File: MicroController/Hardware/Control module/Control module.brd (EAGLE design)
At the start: 100 x 60 mm, 90 parts, among them CN1 JST-PH_2-PIN_HEADER, CN2 JST-PH_2-PIN_HEADER, CN3 JST-PH_2-PIN_HEADER, CN4 JST-PH_2-PIN_HEADER, CN5 JST-PH_2-PIN_HEADER, CN6 JST-PH_2-PIN_HEADER, CN7 JST-PH_2-PIN_HEADER, CN8 JST-PH_2-PIN_HEADER, J1 1X2-3.5MM, J2 RJ45-TRAFO, J3 RJ45-TRAFO, J4 RJ45-TRAFO, J6 RJ11, Q1 BSS138, Q2 BSS138, Q3 BSS138, Q4 BSS138, Q5 BSS138, Q6 BSS138, Q7 BSS138, Q8 BSS138, U1 CD74HC4067SM96, U2 DUAL-OPTOISOLATOR_SOIC8, U3 TLV1117-33CDCY, U4 DUAL-OPTOISOLATOR_SOIC8

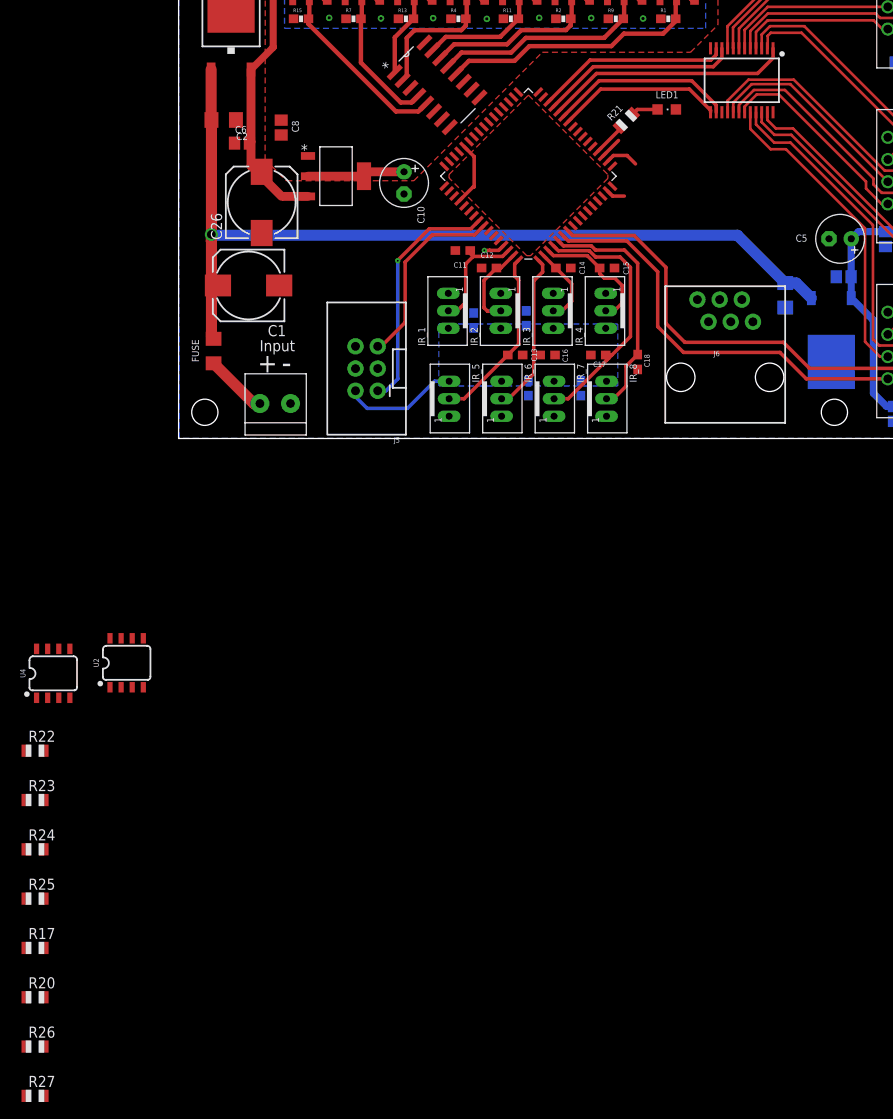
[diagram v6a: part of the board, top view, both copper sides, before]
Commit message: Added the possibility for remote programming.
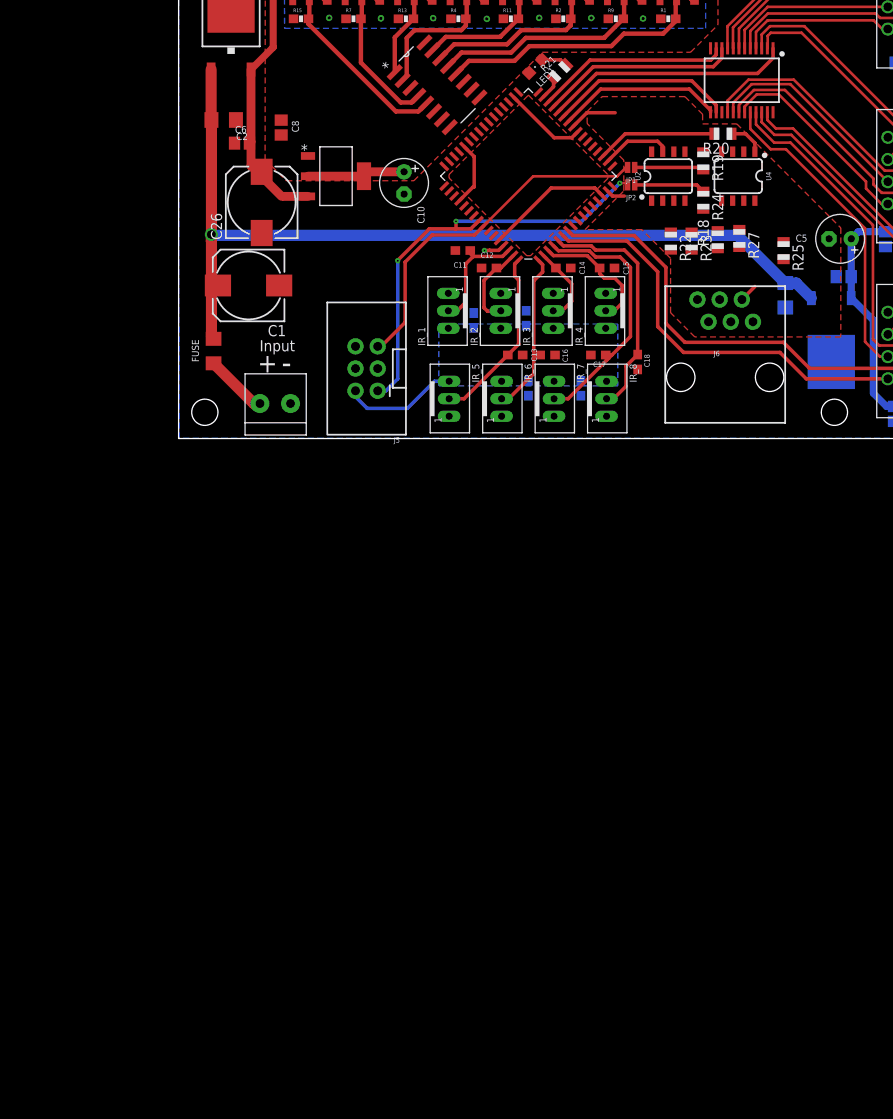
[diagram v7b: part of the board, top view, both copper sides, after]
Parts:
- removed R17, R26: 10K, adafruit:R0805
- added JP1, JP2: JUMPER-SMT_2_NO_NO-SILK, SparkFun-Jumpers:SMT-JUMPER_2_NO_NO-SILK
- added R18, R19: 10K, adafruit:R0805
- moved R27 126.9 mm to (64.1, 22.9), turned to 270 degrees
- moved R20 126.3 mm to (62.2, 34.9), turned to 180 degrees
- moved R25 113.2 mm to (69.2, 21.5), turned to 270 degrees
- moved R24 106.5 mm to (60.0, 27.2), turned to 270 degrees
- moved R23 98.6 mm to (58.7, 22.6), turned to 270 degrees
- moved U4 96.8 mm to (64.0, 30.0), turned to 180 degrees
- moved R22 93.2 mm to (56.3, 22.6), turned to 270 degrees
- moved U2 83.3 mm to (56.0, 30.0)
- moved LED1 15.8 mm to (40.8, 42.6), turned to 135 degrees
- moved R21 9.45 mm to (43.6, 42.0)
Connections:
- removed net N$3 (its old number): R21.2, U$1.20
- removed net SIGNAL_ATXMEGA: R17.2
- removed net SIGNAL_RASPI: J6.5, R26.1, U4.8
- new net DATA_RASPI: J6.5, R25.2
- new net N$1: R21.2, U$1.31
- new net N$4: R20.1, U4.1
- new net N$5: R25.1, U4.3
- net GND: now also R18.1, R19.1, R24.2; no longer U2.5, U2.7, U4.4
- net GND_RASPI: now also R27.2, U4.4; no longer U4.5, U4.7
- net N$2: now also JP1.1, R19.2, U2.5; no longer R17.1, U4.1
- net N$8: now also JP2.1, R24.1, U4.5; no longer R20.1, U4.3
- net PDI_DATA: now also JP2.2
- net RESET_PDI_CLK: now also JP1.2; no longer R24.1, U2.6
- net RX_ATXMEGA: now also R18.2, U2.7; no longer R25.1, U2.8
- net RX_RASPI: now also U4.7; no longer U4.6
- net VCC: now also U2.6, U2.8, U4.6; no longer R24.2, R25.2, R26.2, R27.2
- net VCC_RASPI: now also U4.8
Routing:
- net GND: track 7.49 -> 31.8 mm
- net PDI_DATA: track 27.6 -> 50.0 mm, vias 1 -> 3
- net RESET_PDI_CLK: track 21.9 -> 41.1 mm
- net TX_ATXMEGA: track 2.58 -> 13.8 mm
- net N$8: track 0.00 -> 8.15 mm
- net N$2: track 0.00 -> 7.95 mm
- net VCC: track 29.0 -> 34.5 mm
- net RX_ATXMEGA: track 3.87 -> 8.12 mm
- net N$4: track 0.00 -> 4.08 mm
- net N$3 (its old number): track 3.91 -> 0.00 mm
- net N$1: track 0.00 -> 2.70 mm
- net DATA_RASPI: track 0.00 -> 2.11 mm

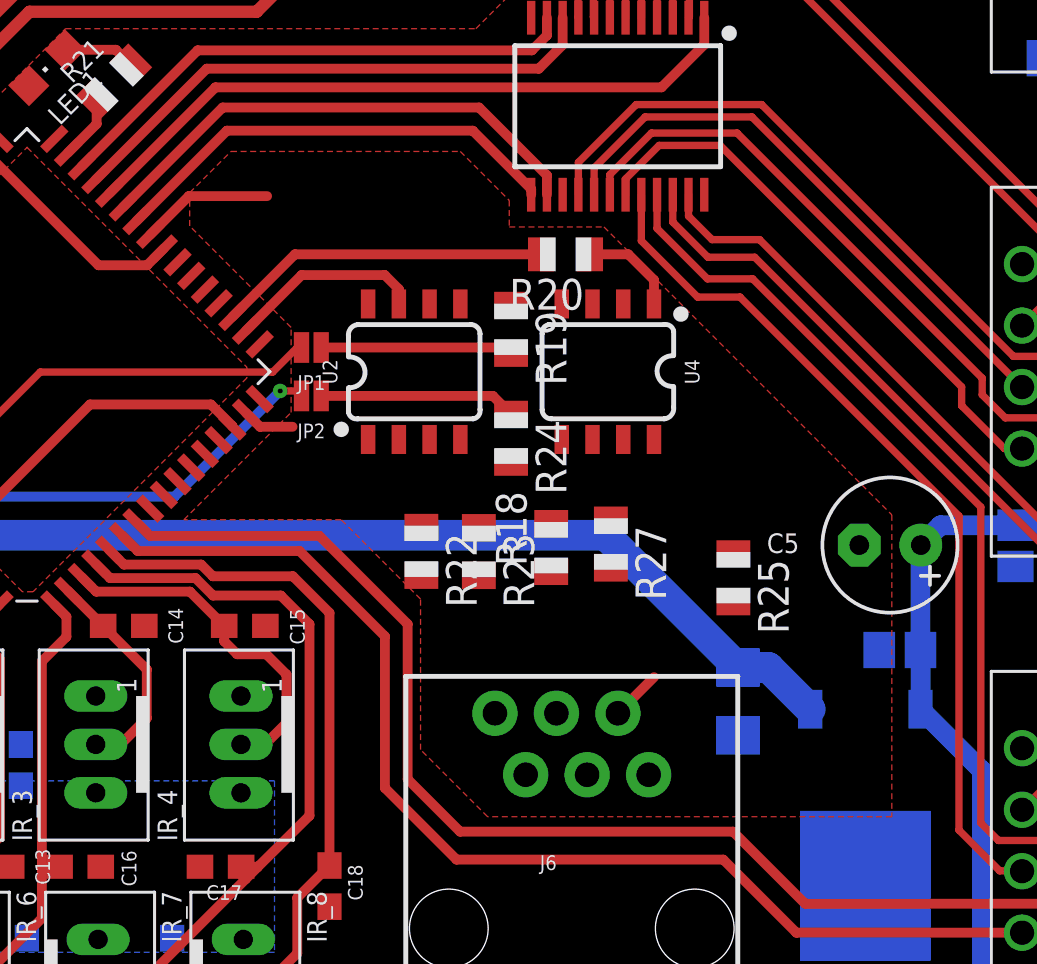
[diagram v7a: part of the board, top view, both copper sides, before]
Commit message: Communication line uses optocouplers for signal seperation.
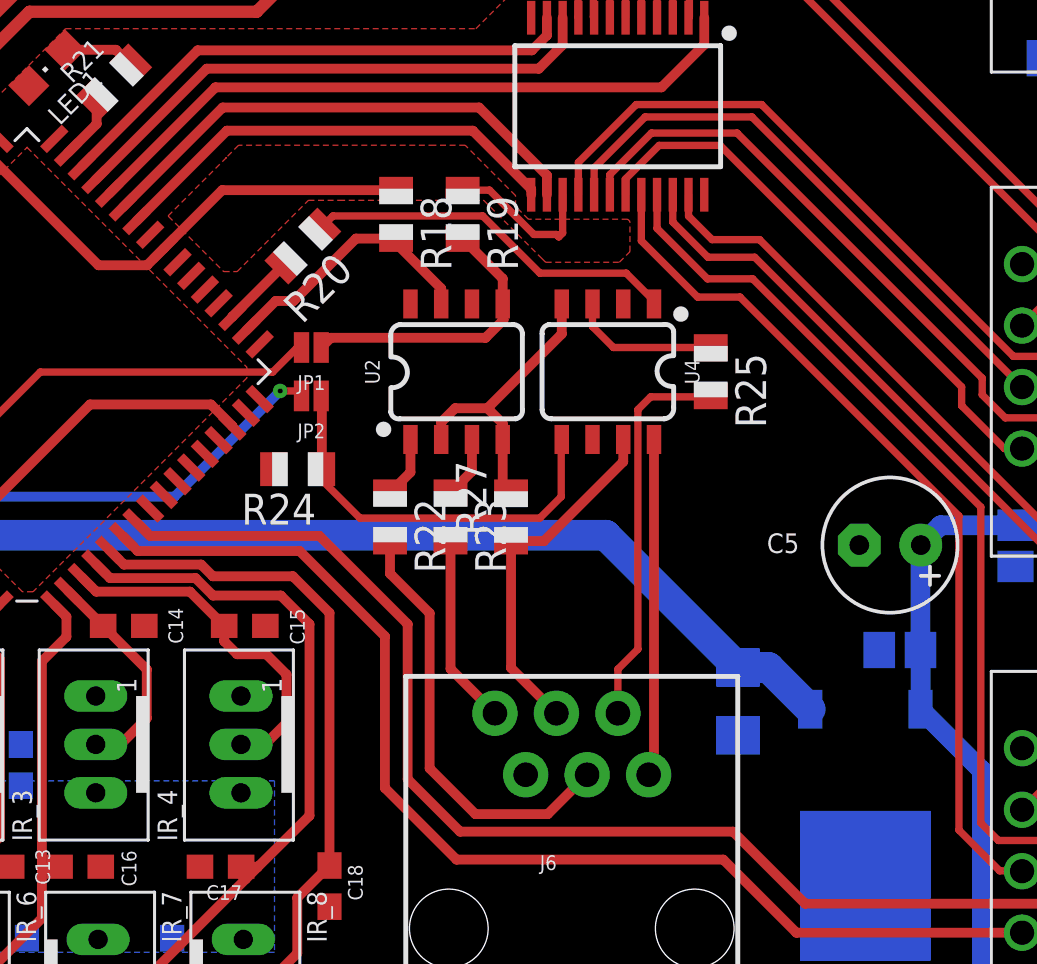
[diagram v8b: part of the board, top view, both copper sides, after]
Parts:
- moved R18 15.2 mm to (55.2, 36.5), turned to 270 degrees
- moved R20 10.9 mm to (51.4, 35.2), turned to 225 degrees
- moved R24 8.91 mm to (51.2, 26.0), turned to 180 degrees
- moved R25 8.57 mm to (68.2, 30.0)
- moved R19 5.15 mm to (58.0, 36.5)
- moved R27 4.27 mm to (60.0, 24.0), turned to 90 degrees
- moved R22 1.92 mm to (55.0, 24.0)
- moved R23 1.85 mm to (57.5, 24.0)
- moved U2 1.75 mm to (57.8, 30.0)
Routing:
- net TX_RASPI: track 0.00 -> 18.0 mm
- net GND: track 31.8 -> 49.0 mm
- net RX_RASPI: track 0.00 -> 14.8 mm
- net DATA_RASPI: track 2.11 -> 16.1 mm
- net VCC_RASPI: track 0.00 -> 13.9 mm
- net GND_RASPI: track 0.00 -> 12.3 mm
- net N$4: track 4.08 -> 15.6 mm
- net TX_ATXMEGA: track 13.8 -> 3.14 mm
- net N$8: track 8.15 -> 16.8 mm
- net RES_RASPI: track 0.00 -> 7.87 mm
- net VCC: track 34.5 -> 26.9 mm
- net N$5: track 0.00 -> 6.18 mm
- net N$2: track 7.95 -> 12.1 mm
- net RX_ATXMEGA: track 8.12 -> 11.2 mm
- net N$7: track 0.00 -> 2.57 mm
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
